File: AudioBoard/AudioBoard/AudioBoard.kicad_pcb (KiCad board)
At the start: 4 copper layers, 250 x 160 mm, 268 parts, among them J1 IN, J2 XLR_L, J3 FX_RETURN, J4 FX_SEND, J5 INS_OUT, J6 XLR_R, J7 Barrel_Jack, J8 NMJ6HFD2, J9 NMJ6HFD2, SW2 SW_SPDT_321, SW3 PWR_SW, U10 TL072, U11 TL072, U12 TL072, U13 TL072, U14 TL072, U15 NJM4556A, U18 NJM4556A, U2 NE5532, U3 NE5532, U4 TL072, U5 TL072, U6 TL072, U7 TL072, U8 TL072, U9 TL072

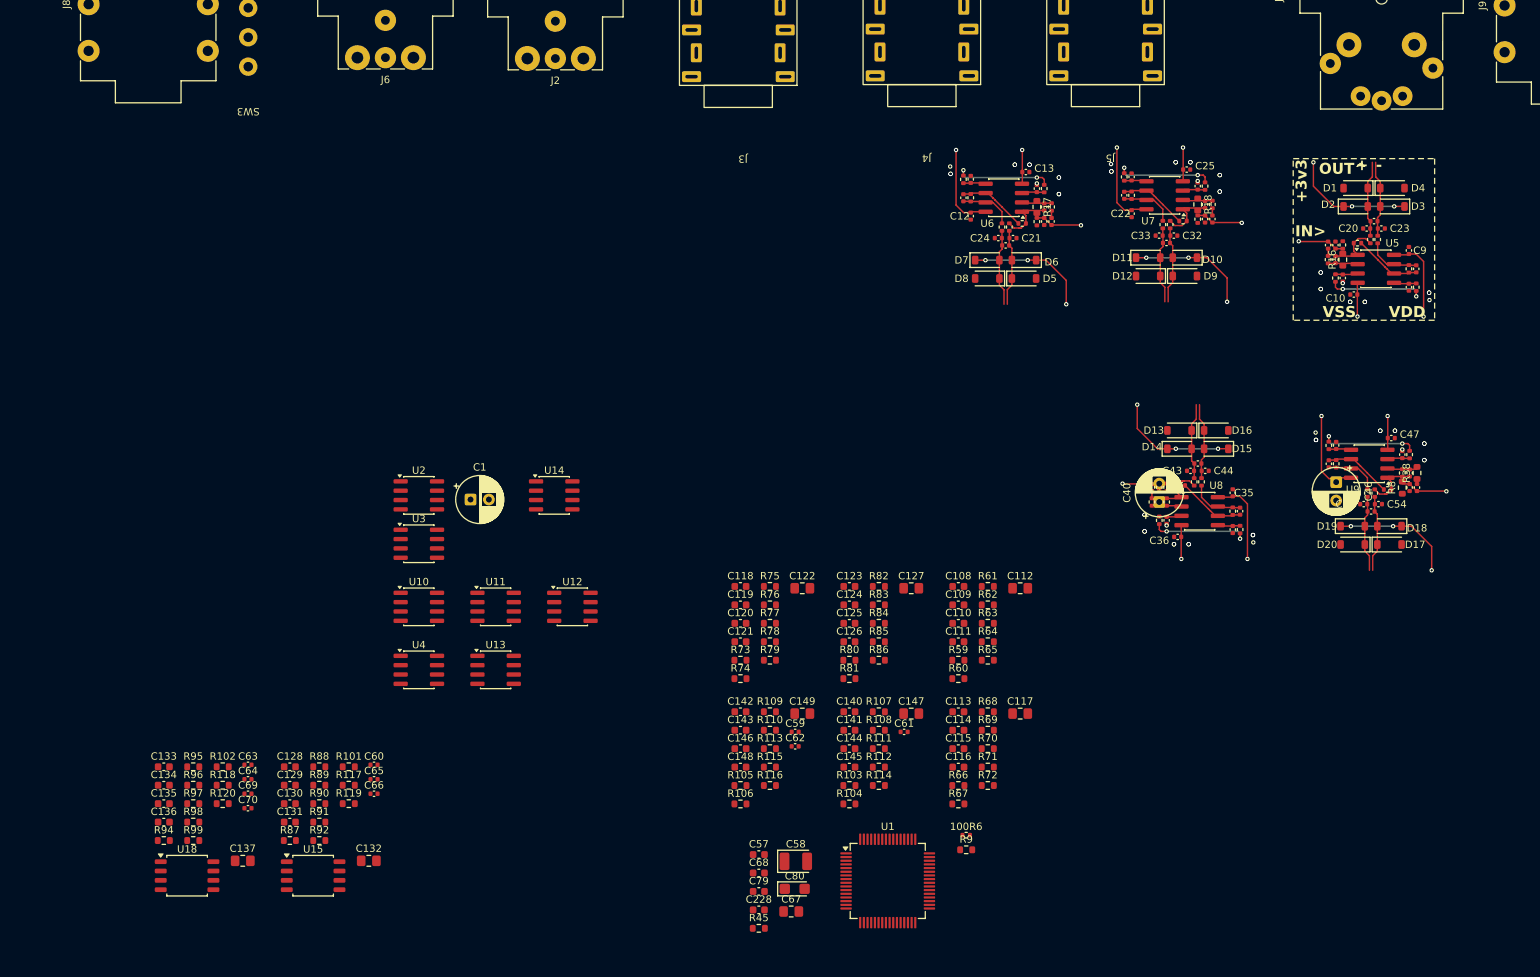
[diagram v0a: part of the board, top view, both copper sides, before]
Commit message: added first time routing to see crosssections
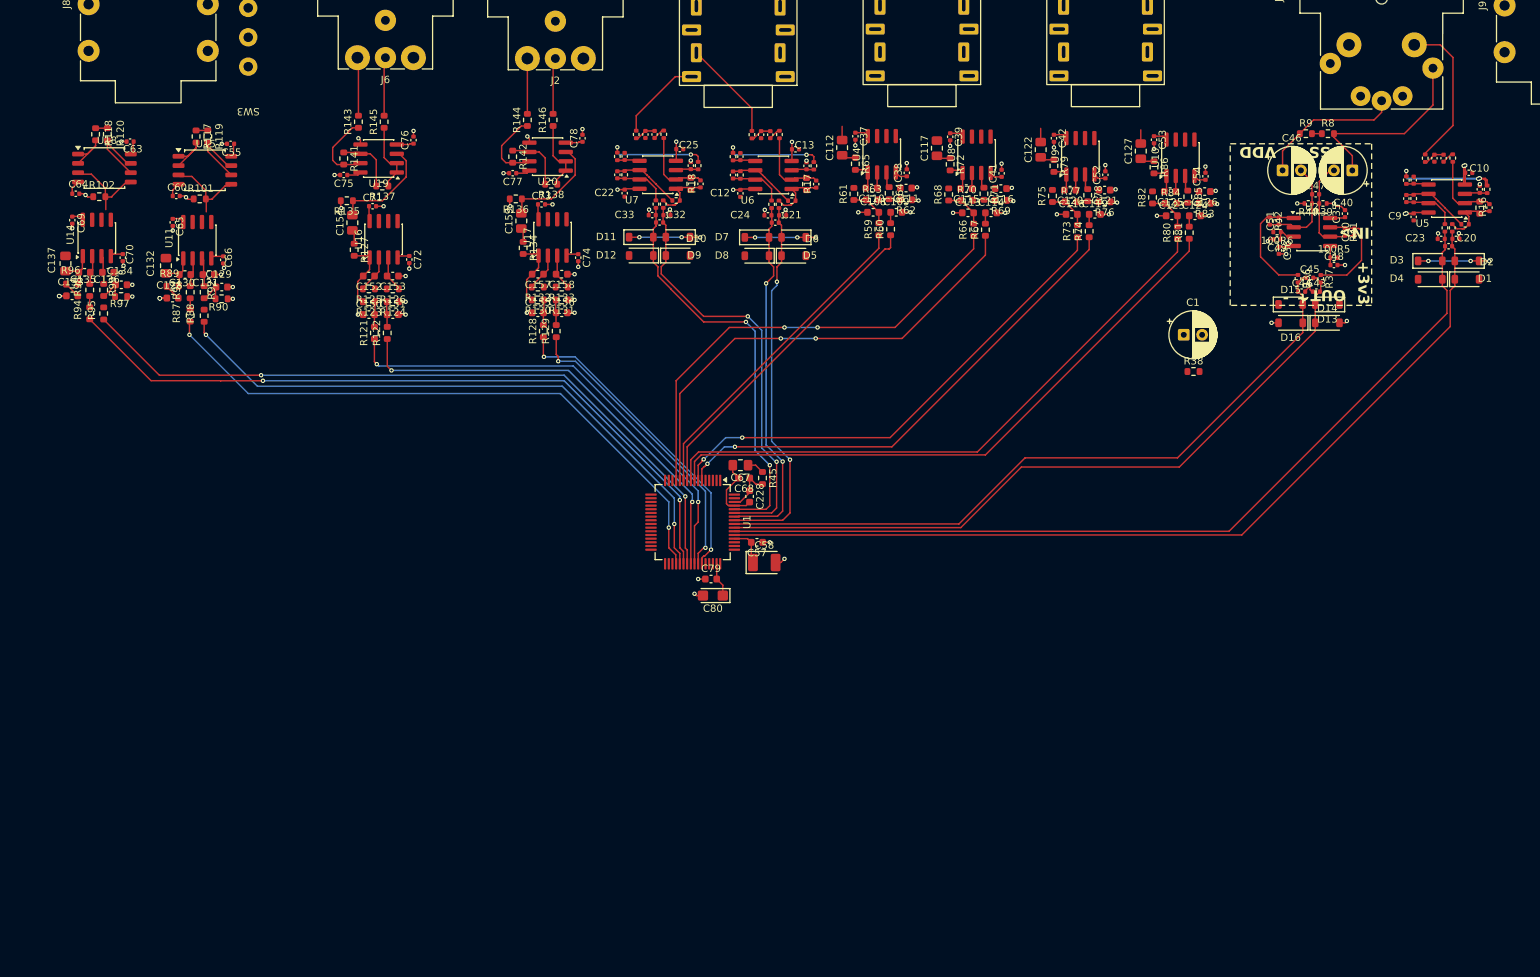
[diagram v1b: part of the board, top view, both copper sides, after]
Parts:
- removed 100R4: 1k, Resistor_SMD:R_0402_1005Metric
- removed C140, C141, C142, C143: 470pF, Capacitor_SMD:C_0603_1608Metric
- removed C144, C145, C146, C148: 100pF, Capacitor_SMD:C_0603_1608Metric
- removed C147, C149: 2.2uF, Capacitor_SMD:C_0805_2012Metric_Pad1.18x1.45mm_HandSolder
- removed C56, C59, C61, C62: 100n, Capacitor_SMD:C_0402_1005Metric
- removed D17, D18, D19, D20: 1N4148W, Diode_SMD:D_SOD-123
- removed R103, R104, R105, R106, R107, R108, R109, R110, R111, R112, R113, R115: 3k, Resistor_SMD:R_0603_1608Metric
- removed R114, R116: 1k, Resistor_SMD:R_0603_1608Metric
- removed R25: 1M, Resistor_SMD:R_0402_1005Metric
- removed R26, R43, R44, R7: 100R, Resistor_SMD:R_0402_1005Metric
- removed R27: 510k, Resistor_SMD:R_0402_1005Metric
- removed R34, R35: 4k7, Resistor_SMD:R_0402_1005Metric
- removed U12, U13: TL072, Package_SO:SOIC-8_3.9x4.9mm_P1.27mm
- removed U3: NE5532, Package_SO:SOIC-8_3.9x4.9mm_P1.27mm
- added C150: 470pF, Capacitor_SMD:C_0603_1608Metric, F.Cu at (127.4, 112.8)
- added C151: 470pF, Capacitor_SMD:C_0603_1608Metric, F.Cu at (130.7, 112.8)
- added C152: 100pF, Capacitor_SMD:C_0603_1608Metric, F.Cu at (127.4, 107.5)
- added C153: 100pF, Capacitor_SMD:C_0603_1608Metric, F.Cu at (130.7, 107.5)
- added C154: 2.2uF, Capacitor_SMD:C_0805_2012Metric_Pad1.18x1.45mm_HandSolder, F.Cu at (125.2, 100.2)
- added C155: 470pF, Capacitor_SMD:C_0603_1608Metric, F.Cu at (150.4, 112.5)
- added C156: 470pF, Capacitor_SMD:C_0603_1608Metric, F.Cu at (153.7, 112.5)
- added C157: 100pF, Capacitor_SMD:C_0603_1608Metric, F.Cu at (150.4, 107.2)
- added C158: 100pF, Capacitor_SMD:C_0603_1608Metric, F.Cu at (153.7, 107.2)
- added C159: 2.2uF, Capacitor_SMD:C_0805_2012Metric_Pad1.18x1.45mm_HandSolder, F.Cu at (148.2, 100.0)
- added C71: 100n, Capacitor_SMD:C_0402_1005Metric, F.Cu at (127.9, 98.0)
- added C72: 100n, Capacitor_SMD:C_0402_1005Metric, F.Cu at (132.9, 105.2)
- added C73: 100n, Capacitor_SMD:C_0402_1005Metric, F.Cu at (150.9, 97.8)
- added C74: 100n, Capacitor_SMD:C_0402_1005Metric, F.Cu at (155.9, 105.0)
- added C75: 100n, Capacitor_SMD:C_0402_1005Metric, F.Cu at (124.0, 93.8)
- added C76: 100n, Capacitor_SMD:C_0402_1005Metric, F.Cu at (133.5, 89.0)
- added C77: 100n, Capacitor_SMD:C_0402_1005Metric, F.Cu at (147.0, 93.5)
- added C78: 100n, Capacitor_SMD:C_0402_1005Metric, F.Cu at (156.5, 88.8)
- added R121: 3k, Resistor_SMD:R_0603_1608Metric, F.Cu at (128.2, 115.2)
- added R122: 3k, Resistor_SMD:R_0603_1608Metric, F.Cu at (129.9, 115.2)
- added R123: 3k, Resistor_SMD:R_0603_1608Metric, F.Cu at (127.4, 111.0)
- added R124: 3k, Resistor_SMD:R_0603_1608Metric, F.Cu at (130.7, 111.0)
- added R125: 3k, Resistor_SMD:R_0603_1608Metric, F.Cu at (127.4, 109.2)
- added R126: 3k, Resistor_SMD:R_0603_1608Metric, F.Cu at (130.7, 109.2)
- added R127: 1k, Resistor_SMD:R_0603_1608Metric, F.Cu at (125.4, 103.9)
- added R128: 3k, Resistor_SMD:R_0603_1608Metric, F.Cu at (151.2, 115.0)
- added R129: 3k, Resistor_SMD:R_0603_1608Metric, F.Cu at (152.9, 115.0)
- added R130: 3k, Resistor_SMD:R_0603_1608Metric, F.Cu at (150.4, 110.8)
- added R131: 3k, Resistor_SMD:R_0603_1608Metric, F.Cu at (153.7, 110.8)
- added R132: 3k, Resistor_SMD:R_0603_1608Metric, F.Cu at (150.4, 109.0)
- added R133: 3k, Resistor_SMD:R_0603_1608Metric, F.Cu at (153.7, 109.0)
- added R134: 1k, Resistor_SMD:R_0603_1608Metric, F.Cu at (148.4, 103.7)
- added R135: 10k, Resistor_SMD:R_0603_1608Metric, F.Cu at (124.4, 97.2)
- added R136: 10k, Resistor_SMD:R_0603_1608Metric, F.Cu at (147.4, 97.0)
- added R137: 10k, Resistor_SMD:R_0603_1608Metric, F.Cu at (129.2, 95.2)
- added R138: 10k, Resistor_SMD:R_0603_1608Metric, F.Cu at (152.2, 95.0)
- added R141: 10k, Resistor_SMD:R_0603_1608Metric, F.Cu at (124.0, 91.5)
- added R142: 10k, Resistor_SMD:R_0603_1608Metric, F.Cu at (147.0, 91.2)
- added R143: 100, Resistor_SMD:R_0603_1608Metric, F.Cu at (126.0, 86.5)
- added R144: 100, Resistor_SMD:R_0603_1608Metric, F.Cu at (149.0, 86.2)
- added R145: 100, Resistor_SMD:R_0603_1608Metric, F.Cu at (129.5, 86.5)
- added R146: 100, Resistor_SMD:R_0603_1608Metric, F.Cu at (152.5, 86.2)
- added U16: TL072, Package_SO:SOIC-8_3.9x4.9mm_P1.27mm, F.Cu at (129.4, 102.5)
- added U17: TL072, Package_SO:SOIC-8_3.9x4.9mm_P1.27mm, F.Cu at (152.4, 102.2)
- added U19: TL072, Package_SO:SOIC-8_3.9x4.9mm_P1.27mm, F.Cu at (128.8, 91.5)
- added U20: TL072, Package_SO:SOIC-8_3.9x4.9mm_P1.27mm, F.Cu at (151.8, 91.2)
- moved C55 161.9 mm to (108.6, 89.5)
- moved U2 126.8 mm to (255.8, 101.5)
- moved U10 120.4 mm to (237.9, 91.4), turned to 90 degrees
- moved R9 107.9 mm to (255.0, 88.1)
- moved C1 99.6 mm to (238.3, 115.5)
- moved U15 97.1 mm to (105.1, 93.1)
- moved U18 97.0 mm to (91.4, 92.8)
- moved U4 94.3 mm to (197.2, 90.9), turned to 90 degrees
- moved R119 92.8 mm to (105.5, 88.5), turned to -90 degrees
- moved R120 92.5 mm to (91.8, 88.2), turned to -90 degrees
- moved 100R6 92.4 mm to (251.1, 101.5), turned to 180 degrees
- moved R117 90.7 mm to (103.9, 88.5), turned to -90 degrees
- moved R118 90.3 mm to (90.2, 88.2), turned to -90 degrees
- moved C63 86.3 mm to (94.9, 89.2), turned to 180 degrees
- moved C132 85.6 mm to (99.8, 106.1), turned to 90 degrees
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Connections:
- 100R6 pad 1: Net-(U3A-+) -> Net-(U2A-+)
- C112 pad 2: /Instrument_output_L/OUT -> /Audio_IO_conn/SEND_2
- C117 pad 2: /Instrument_output_R/OUT -> /Audio_IO_conn/SEND_1
- C122 pad 2: /Instrument_L1_send/OUT -> /Audio_IO_conn/OUT_R
- C127 pad 2: /Instrument_L2_send/OUT -> /Audio_IO_conn/OUT_L
- C46 pad 2: Net-(U3A--) -> Net-(U2A--)
- C47 pad 1: Net-(U3A--) -> Net-(U2A--)
- C49 pad 1: Net-(U3A-+) -> Net-(U2A-+)
- C51 pad 1: Net-(U3A--) -> Net-(U2A--)
- J9 pad T: /Audio_IO_conn/EXP_PWR -> DVDD
- R117 pad 1: /HeadphoneAmplifier/OUT -> /Audio_IO_conn/HEADPHONE_R
- R118 pad 1: /HeadphoneAmplifier1/OUT -> /Audio_IO_conn/HEADPHONE_L
- R119 pad 1: /HeadphoneAmplifier/OUT -> /Audio_IO_conn/HEADPHONE_R
- R120 pad 1: /HeadphoneAmplifier1/OUT -> /Audio_IO_conn/HEADPHONE_L
- R40 pad 1: Net-(U3A--) -> Net-(U2A--)
- R42 pad 2: Net-(U3A--) -> Net-(U2A--)
- R5 pad 1: /Instrument_L1_return/IN -> /Audio_IO_conn/RET_1
- R6 pad 1: /Instrument_L2_return/IN -> /Audio_IO_conn/RET_2
- U1 pad 10: /HeadphoneAmplifier1/IN_P -> /Instrument_output_L/IN_N
- U1 pad 11: /HeadphoneAmplifier1/IN_N -> /Instrument_output_L/IN_P
- U1 pad 12: /HeadphoneAmplifier/IN_P -> /Instrument_output_R/IN_N
- U1 pad 13: /HeadphoneAmplifier/IN_N -> /Instrument_output_R/IN_P
- U1 pad 36: /Instrument_output_R/IN_P -> /HeadphoneAmplifier/IN_N
- U1 pad 37: /Instrument_output_R/IN_N -> /HeadphoneAmplifier/IN_P
- U1 pad 38: /Instrument_output_L/IN_P -> /HeadphoneAmplifier1/IN_N
- U1 pad 39: /Instrument_output_L/IN_N -> /HeadphoneAmplifier1/IN_P
- U1 pad 40: /Instrument_L2_send/IN_P -> /XLR_output_L/IN_N_N
- U1 pad 41: /Instrument_L2_send/IN_N -> /XLR_output_L/IN_N_P
- U1 pad 42: /Instrument_L1_send/IN_P -> /XLR_output_R/IN_N_N
- U1 pad 43: /Instrument_L1_send/IN_N -> /XLR_output_R/IN_N_P
- U1 pad 6: /XLR_output_R/IN_N_P -> /Instrument_L1_send/IN_N
- U1 pad 7: /XLR_output_R/IN_N_N -> /Instrument_L1_send/IN_P
- U1 pad 8: /XLR_output_L/IN_N_P -> /Instrument_L2_send/IN_N
- U1 pad 9: /XLR_output_L/IN_N_N -> /Instrument_L2_send/IN_P
- U2 pad 1: (no net) -> Net-(C51-Pad2)
- U2 pad 2: (no net) -> Net-(U2A--)
- U2 pad 3: (no net) -> Net-(U2A-+)
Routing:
- net /Instrument_Input/OUT_P: track 10.4 -> 122.6 mm
- net /Instrument_Input/OUT_N: track 10.4 -> 120.9 mm
- net /HeadphoneAmplifier1/IN_N: track 0.00 -> 99.7 mm, vias 0 -> 2
- net /HeadphoneAmplifier1/IN_P: track 0.00 -> 98.4 mm, vias 0 -> 2
- net /MIC_preamp/OUT_P: track 10.4 -> 98.4 mm
- net /MIC_preamp/OUT_N: track 10.4 -> 96.6 mm
- net /HeadphoneAmplifier/IN_N: track 0.00 -> 85.4 mm, vias 0 -> 2
- net /HeadphoneAmplifier/IN_P: track 0.00 -> 84.1 mm, vias 0 -> 2
- net /Instrument_L2_send/IN_N: track 0.00 -> 83.5 mm
- net /Instrument_L2_send/IN_P: track 0.00 -> 82.6 mm
- net /Instrument_L1_send/IN_N: track 0.00 -> 68.3 mm, vias 0 -> 2
- net /Instrument_L1_send/IN_P: track 0.00 -> 67.6 mm, vias 0 -> 2
- net /XLR_output_L/IN_N_P: track 0.00 -> 64.6 mm, vias 0 -> 2
- net /Instrument_output_R/IN_N: track 0.00 -> 63.9 mm, vias 0 -> 2
- net GND: track 15.7 -> 79.1 mm, vias 61 -> 83
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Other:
- board text added: "INPUT"
- board text added: "OUTPUT"
